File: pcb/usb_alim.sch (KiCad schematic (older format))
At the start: 0 parts

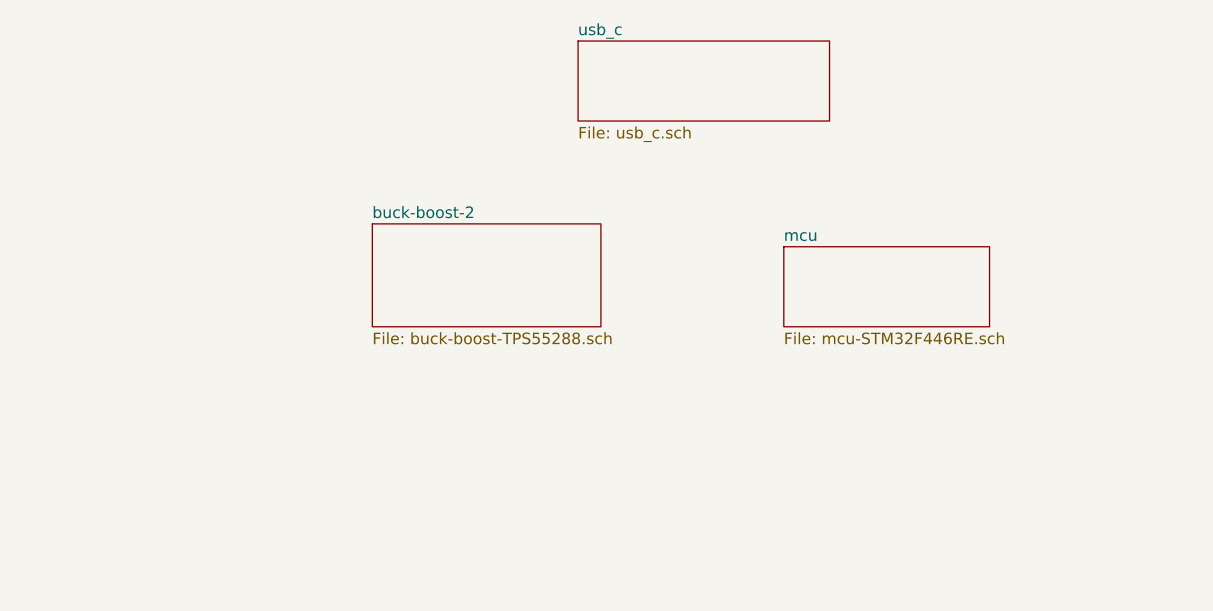
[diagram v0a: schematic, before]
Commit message: [PCB] update mcu config & pwr converter, add sd card
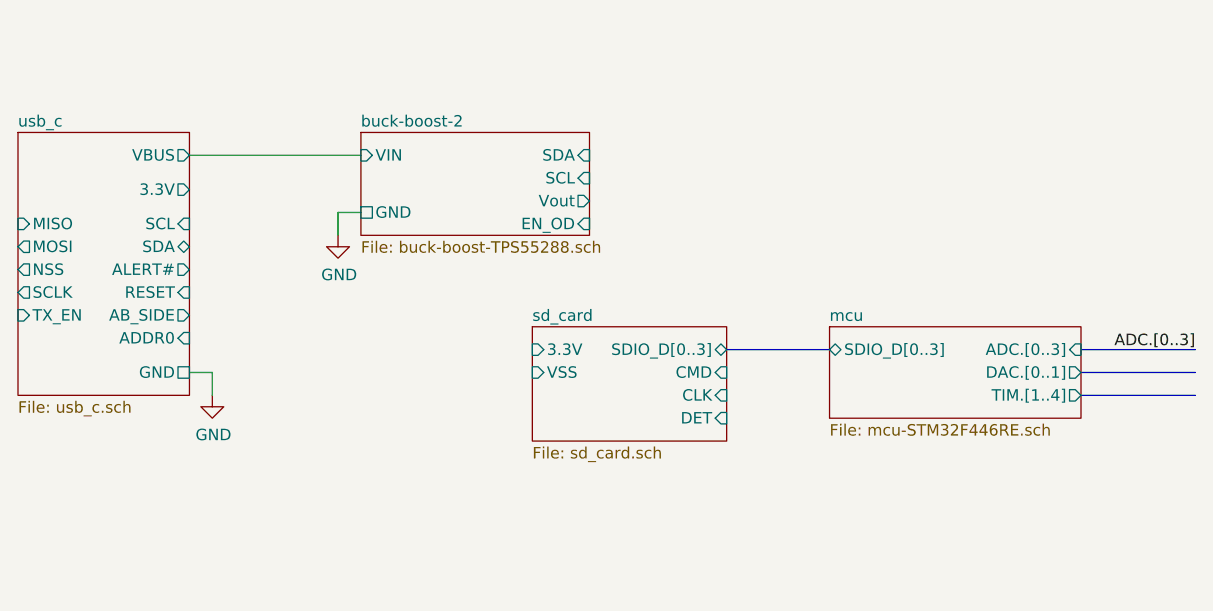
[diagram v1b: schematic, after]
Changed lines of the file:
@@
 $Descr A4 11693 8268
 encoding utf-8
-Sheet 1 4
+Sheet 1 5
 Title ""
 Date ""
@@
 $EndDescr
 $Sheet
-S 4100 3350 1000 450
+S 4050 2950 1000 450
 U 605D4A93
 F0 "buck-boost-2" 50
 F1 "buck-boost-TPS55288.sch" 50
+F2 "VIN" I L 4050 3050 50
+F3 "GND" U L 4050 3300 50
+F4 "Vout" O R 5050 3250 50
+F5 "SCL" I R 5050 3150 50
+F6 "SDA" I R 5050 3050 50
+F7 "EN_OD" I R 5050 3350 50
 $EndSheet
 $Sheet
-S 5900 3450 900  350
+S 2550 2950 750  1150
+U 6071A9E5
+F0 "usb_c" 50
+F1 "usb_c.sch" 50
+F2 "MISO" I L 2550 3350 50
+F3 "MOSI" O L 2550 3450 50
+F4 "NSS" O L 2550 3550 50
+F5 "SCLK" O L 2550 3650 50
+F6 "TX_EN" I L 2550 3750 50
+F7 "SCL" I R 3300 3350 50
+F8 "SDA" B R 3300 3450 50
+F9 "ALERT#" O R 3300 3550 50
+F10 "RESET" I R 3300 3650 50
+F11 "AB_SIDE" O R 3300 3750 50
+F12 "ADDR0" I R 3300 3850 50
+F13 "3.3V" O R 3300 3200 50
+F14 "VBUS" O R 3300 3050 50
+F15 "GND" U R 3300 4000 50
+$EndSheet
+Wire Wire Line
+	3300 3050 4050 3050
+$Comp
+L power:GND #PWR0101
+U 1 1 608E7C13
+P 3400 4100
+F 0 "#PWR0101" H 3400 3850 50  0001 C CNN
+F 1 "GND" H 3405 3927 50  0000 C CNN
+F 2 "" H 3400 4100 50  0001 C CNN
+F 3 "" H 3400 4100 50  0001 C CNN
+	1    3400 4100
+	1    0    0    -1
+$EndComp
+Wire Wire Line
+	3300 4000 3400 4000
+Wire Wire Line
+	3400 4000 3400 4100
+$Comp
+L power:GND #PWR0102
+U 1 1 608E7FC6
+P 3950 3400
+F 0 "#PWR0102" H 3950 3150 50  0001 C CNN
+F 1 "GND" H 3955 3227 50  0000 C CNN
+F 2 "" H 3950 3400 50  0001 C CNN
+F 3 "" H 3950 3400 50  0001 C CNN
+	1    3950 3400
+	1    0    0    -1
+$EndComp
+Wire Wire Line
+	4050 3300 3950 3300
+Wire Wire Line
+	3950 3300 3950 3400
+Wire Bus Line
+	7200 4000 7700 4000
+Wire Bus Line
+	7200 4100 7700 4100
+Text Label 7700 3900 2    50   ~ 0
+ADC.[0..3]
+Wire Bus Line
+	7200 3900 7700 3900
+$Sheet
+S 6100 3800 1100 400
 U 605E3BAB
 F0 "mcu" 50
 F1 "mcu-STM32F446RE.sch" 50
+F2 "DAC.[0..1]" O R 7200 4000 50
+F3 "TIM.[1..4]" O R 7200 4100 50
+F4 "SDIO_D[0..3]" B L 6100 3900 50
+F5 "ADC.[0..3]" I R 7200 3900 50
 $EndSheet
 $Sheet
-S 5000 2550 1100 350
-U 6071A9E5
-F0 "usb_c" 50
-F1 "usb_c.sch" 50
+S 4800 3800 850  500
+U 61165BBE
+F0 "sd_card" 50
+F1 "sd_card.sch" 50
+F2 "SDIO_D[0..3]" B R 5650 3900 50
+F3 "3.3V" I L 4800 3900 50
+F4 "CMD" I R 5650 4000 50
+F5 "CLK" I R 5650 4100 50
+F6 "VSS" I L 4800 4000 50
+F7 "DET" I R 5650 4200 50
 $EndSheet
+Wire Bus Line
+	6100 3900 5650 3900
 $EndSCHEMATC

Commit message: [PCB] minor changes
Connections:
- net labels added: +3.3V, I2C1_SCL, I2C1_SDA, I2C1_SMBA, SPI1_CLK, SPI1_MISO, SPI1_MOSI, SPI1_NSS
- wire segments 5 -> 26
